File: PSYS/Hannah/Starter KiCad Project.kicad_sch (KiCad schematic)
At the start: 14 parts, among them U1 STM32WB55CEUx

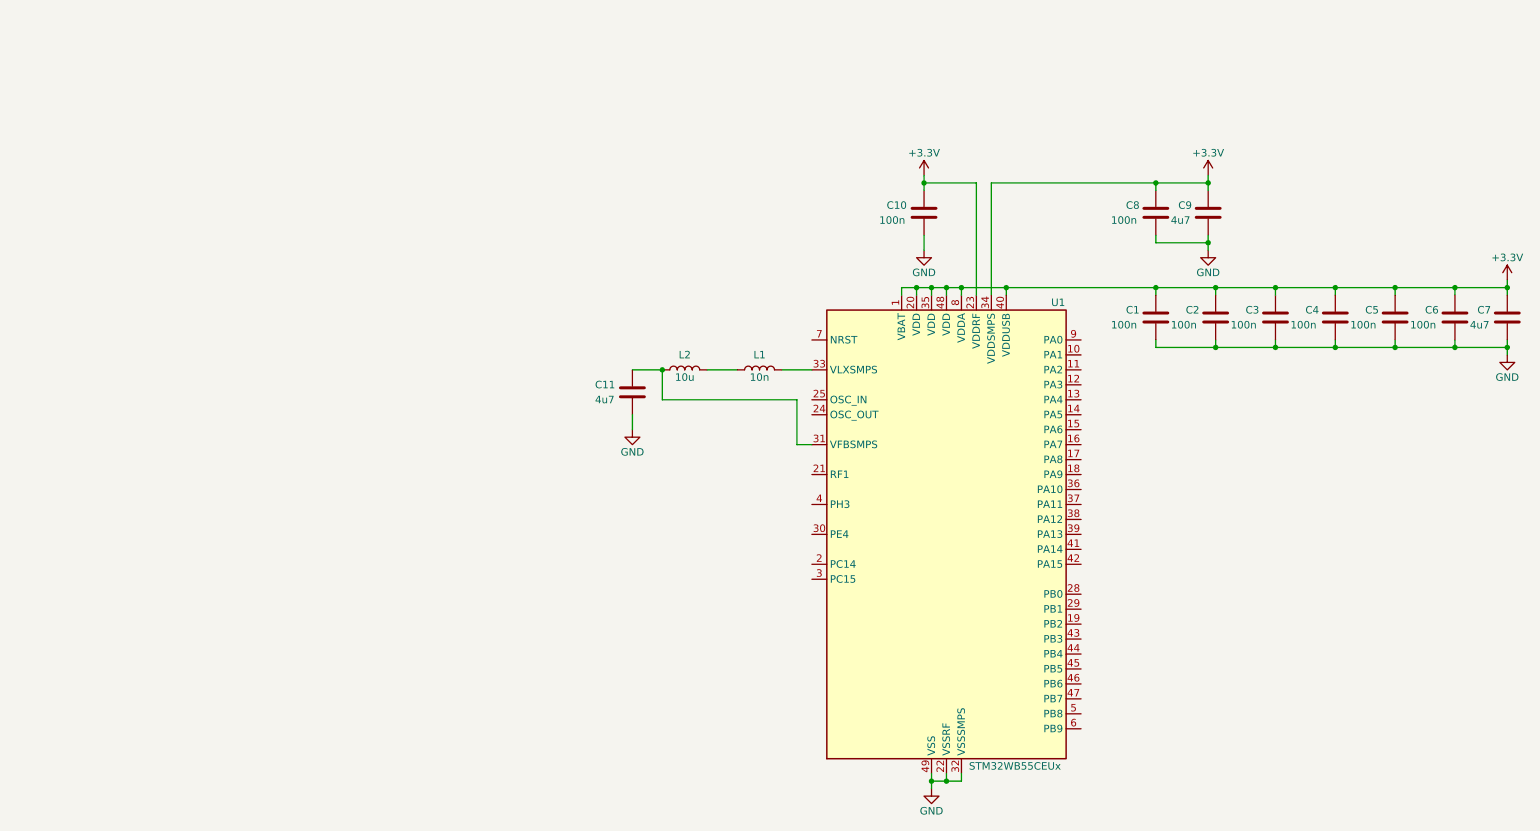
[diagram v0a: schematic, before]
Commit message: mcu mse & lse crystals
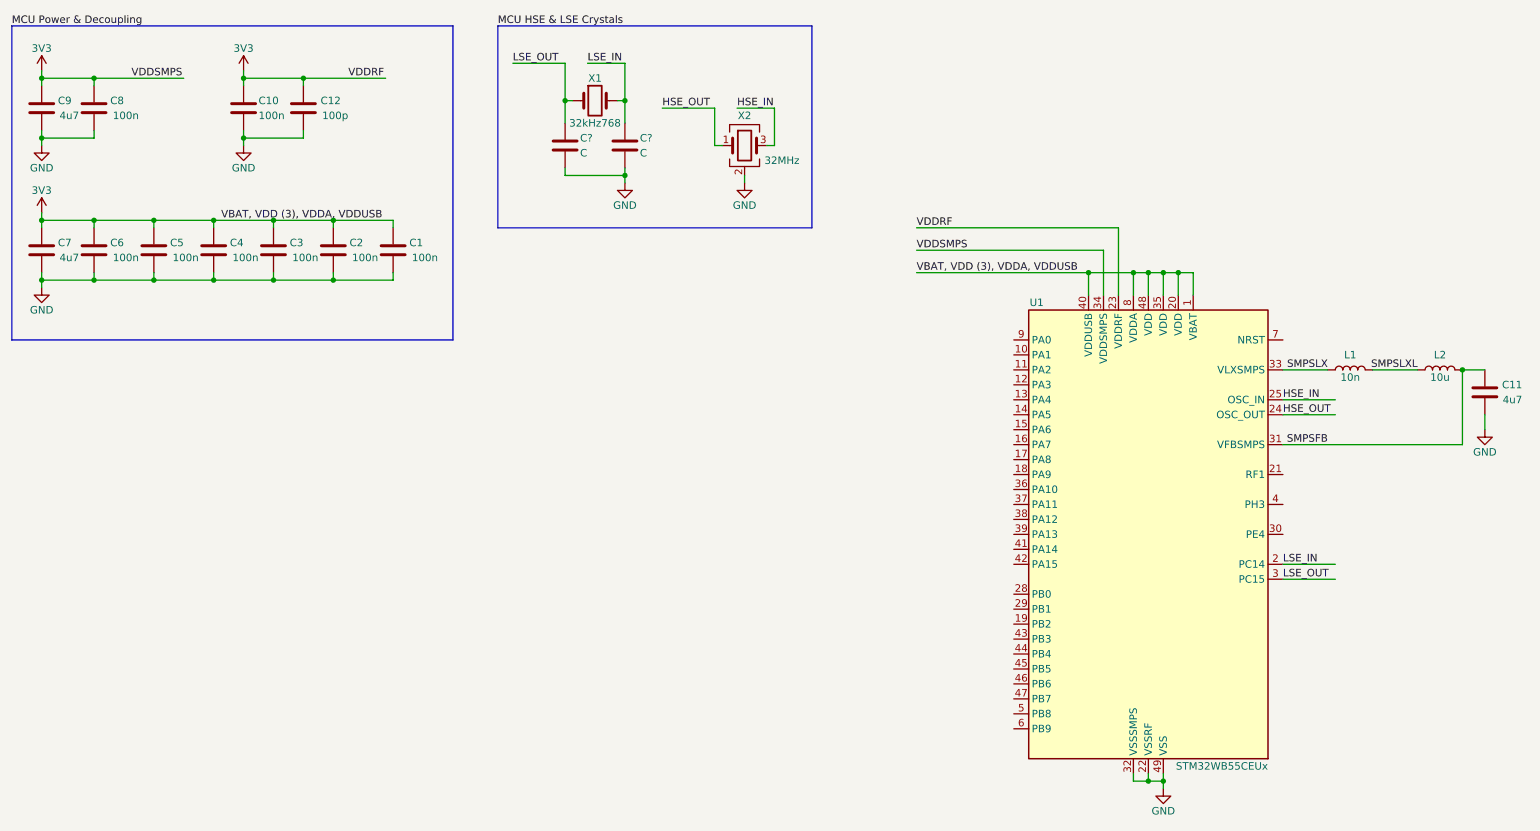
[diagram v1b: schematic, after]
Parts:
- added C12: 100p, symbol Device:C
- added C? (x2): C, symbol Device:C
- added X1: 32kHz768, symbol Device:Crystal
- added X2: 32MHz, symbol Device:Crystal_GND24
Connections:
- net GND: now also C12.2, C?.2, C?.2, X2.2 (G), X2.4 (G)
- net SMPSFB: now reaches C11.1, L2.1, U1.31 (VFBSMPS)
- net SMPSLXL: now reaches L1.1, L2.2
- net LSE_IN: now reaches U1.2 (PC14)
- net LSE_IN: now also C?.1, X1.2
- net HSE_OUT: now reaches U1.24 (OSC_OUT)
- net HSE_OUT: now also X2.1
- net HSE_IN: now reaches U1.25 (OSC_IN)
- net HSE_IN: now also X2.3
- net LSE_OUT: now reaches U1.3 (PC15)
- net LSE_OUT: now also C?.1, X1.1
- net SMPSLX: now reaches L1.2, U1.33 (VLXSMPS)
- net +3.3V renamed 3V3
- net 3V3: now also C12.1
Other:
- moved on the sheet: C1, C10, C11, C2, C3, C4, C5, C6, C7, C8, C9, L1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
